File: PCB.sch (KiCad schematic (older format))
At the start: 62 parts, among them J1 PASSIVE_CHANNELS, J10 USB_RASPBERRY, J11 USB_ARDUINO, J12 100W_ch+, J13 100W_ch-, J14 100W_sense, J2 PASSIVE_CHANNELS, J3 PASSIVE_CHANNELS, J4 12V+, J5 12V-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

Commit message: Placement canal passif intial
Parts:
- renumbered J3 to J1, J1 to J2, J2 to J3
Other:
- moved on the sheet: J1, J2
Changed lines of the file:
@@
 $EndComp
 $Comp
-L Connector:Screw_Terminal_01x16 J2
+L Connector:Screw_Terminal_01x16 J3
 U 1 1 5F3E87B3
 P 1200 16150
-F 0 "J2" H 1118 17067 50  0000 C CNN
+F 0 "J3" H 1118 17067 50  0000 C CNN
 F 1 "PASSIVE_CHANNELS" H 1118 16976 50  0000 C CNN
 F 2 "TerminalBlock_Phoenix:TerminalBlock_Phoenix_PT-1,5-16-5.0-H_1x16_P5.00mm_Horizontal" H 1200 16150 50  0001 C CNN
@@
 $EndComp
 $Comp
-L Connector:Screw_Terminal_01x16 J3
+L Connector:Screw_Terminal_01x16 J1
 U 1 1 5F02987D
-P 1400 3800
-F 0 "J3" H 1318 4717 50  0000 C CNN
-F 1 "PASSIVE_CHANNELS" H 1318 4626 50  0000 C CNN
-F 2 "TerminalBlock_Phoenix:TerminalBlock_Phoenix_PT-1,5-16-5.0-H_1x16_P5.00mm_Horizontal" H 1400 3800 50  0001 C CNN
-F 3 "~" H 1400 3800 50  0001 C CNN
-	1    1400 3800
+P 850 2900
+F 0 "J1" H 768 3817 50  0000 C CNN
+F 1 "PASSIVE_CHANNELS" H 768 3726 50  0000 C CNN
+F 2 "TerminalBlock_Phoenix:TerminalBlock_Phoenix_PT-1,5-16-5.0-H_1x16_P5.00mm_Horizontal" H 850 2900 50  0001 C CNN
+F 3 "~" H 850 2900 50  0001 C CNN
+	1    850  2900
 	-1   0    0    -1
 $EndComp
@@
 T8-
 Wire Wire Line
-	1600 3100 1950 3100
-Wire Wire Line
-	1600 3200 1950 3200
-Text Label 1950 3100 0    50   ~ 0
+	1050 2200 1400 2200
+Wire Wire Line
+	1050 2300 1400 2300
+Text Label 1400 2200 0    50   ~ 0
 T1+
-Text Label 1950 3200 0    50   ~ 0
+Text Label 1400 2300 0    50   ~ 0
 T1-
 Wire Wire Line
-	1600 3300 1950 3300
-Wire Wire Line
-	1600 3400 1950 3400
-Text Label 1950 3300 0    50   ~ 0
+	1050 2400 1400 2400
+Wire Wire Line
+	1050 2500 1400 2500
+Text Label 1400 2400 0    50   ~ 0
 T2+
-Text Label 1950 3400 0    50   ~ 0
+Text Label 1400 2500 0    50   ~ 0
 T2-
 Wire Wire Line
-	1600 3500 1950 3500
-Wire Wire Line
-	1600 3600 1950 3600
-Text Label 1950 3500 0    50   ~ 0
+	1050 2600 1400 2600
+Wire Wire Line
+	1050 2700 1400 2700
+Text Label 1400 2600 0    50   ~ 0
 T3+
-Text Label 1950 3600 0    50   ~ 0
+Text Label 1400 2700 0    50   ~ 0
 T3-
 Wire Wire Line
-	1600 3700 1950 3700
-Wire Wire Line
-	1600 3800 1950 3800
-Text Label 1950 3700 0    50   ~ 0
+	1050 2800 1400 2800
+Wire Wire Line
+	1050 2900 1400 2900
+Text Label 1400 2800 0    50   ~ 0
 T4+
-Text Label 1950 3800 0    50   ~ 0
+Text Label 1400 2900 0    50   ~ 0
 T4-
 Wire Wire Line
-	1600 3900 1950 3900
-Wire Wire Line
-	1600 4000 1950 4000
-Text Label 1950 3900 0    50   ~ 0
+	1050 3000 1400 3000
+Wire Wire Line
+	1050 3100 1400 3100
+Text Label 1400 3000 0    50   ~ 0
 T5+
-Text Label 1950 4000 0    50   ~ 0
+Text Label 1400 3100 0    50   ~ 0
 T5-
 Wire Wire Line
-	1600 4100 1950 4100
-Wire Wire Line
-	1600 4200 1950 4200
-Text Label 1950 4100 0    50   ~ 0
+	1050 3200 1400 3200
+Wire Wire Line
+	1050 3300 1400 3300
+Text Label 1400 3200 0    50   ~ 0
 T6+
-Text Label 1950 4200 0    50   ~ 0
+Text Label 1400 3300 0    50   ~ 0
 T6-
 Wire Wire Line
-	1600 4300 1950 4300
-Wire Wire Line
-	1600 4400 1950 4400
-Text Label 1950 4300 0    50   ~ 0
+	1050 3400 1400 3400
+Wire Wire Line
+	1050 3500 1400 3500
+Text Label 1400 3400 0    50   ~ 0
 T7+
-Text Label 1950 4400 0    50   ~ 0
+Text Label 1400 3500 0    50   ~ 0
 T7-
 Wire Wire Line
-	1600 4500 1950 4500
-Wire Wire Line
-	1600 4600 1950 4600
-Text Label 1950 4500 0    50   ~ 0
+	1050 3600 1400 3600
+Wire Wire Line
+	1050 3700 1400 3700
+Text Label 1400 3600 0    50   ~ 0
 T8+
-Text Label 1950 4600 0    50   ~ 0
+Text Label 1400 3700 0    50   ~ 0
 T8-
 $Comp
-L Connector:Screw_Terminal_01x16 J1
+L Connector:Screw_Terminal_01x16 J2
 U 1 1 5F91A19D
-P 1100 7900
-F 0 "J1" H 1018 8817 50  0000 C CNN
-F 1 "PASSIVE_CHANNELS" H 1018 8726 50  0000 C CNN
-F 2 "TerminalBlock_Phoenix:TerminalBlock_Phoenix_PT-1,5-16-5.0-H_1x16_P5.00mm_Horizontal" H 1100 7900 50  0001 C CNN
-F 3 "~" H 1100 7900 50  0001 C CNN
-	1    1100 7900
+P 850 4800
+F 0 "J2" H 768 5717 50  0000 C CNN
+F 1 "PASSIVE_CHANNELS" H 768 5626 50  0000 C CNN
+F 2 "TerminalBlock_Phoenix:TerminalBlock_Phoenix_PT-1,5-16-5.0-H_1x16_P5.00mm_Horizontal" H 850 4800 50  0001 C CNN
+F 3 "~" H 850 4800 50  0001 C CNN
+	1    850  4800
 	-1   0    0    -1
 $EndComp
 Wire Wire Line
-	1300 7200 1650 7200
-Wire Wire Line
-	1300 7300 1650 7300
-Text Label 1650 7200 0    50   ~ 0
+	1050 4100 1400 4100
+Wire Wire Line
+	1050 4200 1400 4200
+Text Label 1400 4100 0    50   ~ 0
 T9+
-Text Label 1650 7300 0    50   ~ 0
+Text Label 1400 4200 0    50   ~ 0
 T9-
 Wire Wire Line
-	1300 7400 1650 7400
-Wire Wire Line
-	1300 7500 1650 7500
-Text Label 1650 7400 0    50   ~ 0
+	1050 4300 1400 4300
+Wire Wire Line
+	1050 4400 1400 4400
+Text Label 1400 4300 0    50   ~ 0
 T10+
-Text Label 1650 7500 0    50   ~ 0
+Text Label 1400 4400 0    50   ~ 0
 T10-
 Wire Wire Line
-	1300 7600 1650 7600
-Wire Wire Line
-	1300 7700 1650 7700
-Text Label 1650 7600 0    50   ~ 0
+	1050 4500 1400 4500
+Wire Wire Line
+	1050 4600 1400 4600
+Text Label 1400 4500 0    50   ~ 0
 T11+
-Text Label 1650 7700 0    50   ~ 0
+Text Label 1400 4600 0    50   ~ 0
 T11-
 Wire Wire Line
-	1300 7800 1650 7800
-Wire Wire Line
-	1300 7900 1650 7900
-Text Label 1650 7800 0    50   ~ 0
+	1050 4700 1400 4700
+Wire Wire Line
+	1050 4800 1400 4800
+Text Label 1400 4700 0    50   ~ 0
 T12+
-Text Label 1650 7900 0    50   ~ 0
+Text Label 1400 4800 0    50   ~ 0
 T12-
 Wire Wire Line
-	1300 8000 1650 8000
-Wire Wire Line
-	1300 8100 1650 8100
-Text Label 1650 8000 0    50   ~ 0
+	1050 4900 1400 4900
+Wire Wire Line
+	1050 5000 1400 5000
+Text Label 1400 4900 0    50   ~ 0
 T13+
-Text Label 1650 8100 0    50   ~ 0
+Text Label 1400 5000 0    50   ~ 0
 T13-
 Wire Wire Line
-	1300 8200 1650 8200
-Wire Wire Line
-	1300 8300 1650 8300
-Text Label 1650 8200 0    50   ~ 0
+	1050 5100 1400 5100
+Wire Wire Line
+	1050 5200 1400 5200
+Text Label 1400 5100 0    50   ~ 0
 T14+
-Text Label 1650 8300 0    50   ~ 0
+Text Label 1400 5200 0    50   ~ 0
 T14-
 Wire Wire Line
-	1300 8400 1650 8400
-Wire Wire Line
-	1300 8500 1650 8500
-Text Label 1650 8400 0    50   ~ 0
+	1050 5300 1400 5300
+Wire Wire Line
+	1050 5400 1400 5400
+Text Label 1400 5300 0    50   ~ 0
 T15+
-Text Label 1650 8500 0    50   ~ 0
+Text Label 1400 5400 0    50   ~ 0
 T15-
 Wire Wire Line
-	1300 8600 1650 8600
-Wire Wire Line
-	1300 8700 1650 8700
-Text Label 1650 8600 0    50   ~ 0
+	1050 5500 1400 5500
+Wire Wire Line
+	1050 5600 1400 5600
+Text Label 1400 5500 0    50   ~ 0
 T16+
-Text Label 1650 8700 0    50   ~ 0
+Text Label 1400 5600 0    50   ~ 0
 T16-
 Wire Wire Line

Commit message: Defi releve!
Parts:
- D1: footprint Package_TO_SOT_SMD:TO-277A -> PCB:TO-277A
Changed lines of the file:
@@
 F 0 "D1" H 11750 2915 50  0000 C CNN
 F 1 "FSV1045V" H 11750 2824 50  0000 C CNN
-F 2 "Package_TO_SOT_SMD:TO-277A" H 11750 2650 50  0001 C CNN
+F 2 "PCB:TO-277A" H 11750 2650 50  0001 C CNN
 F 3 "~" H 11750 2650 50  0001 C CNN
 	1    11750 2650

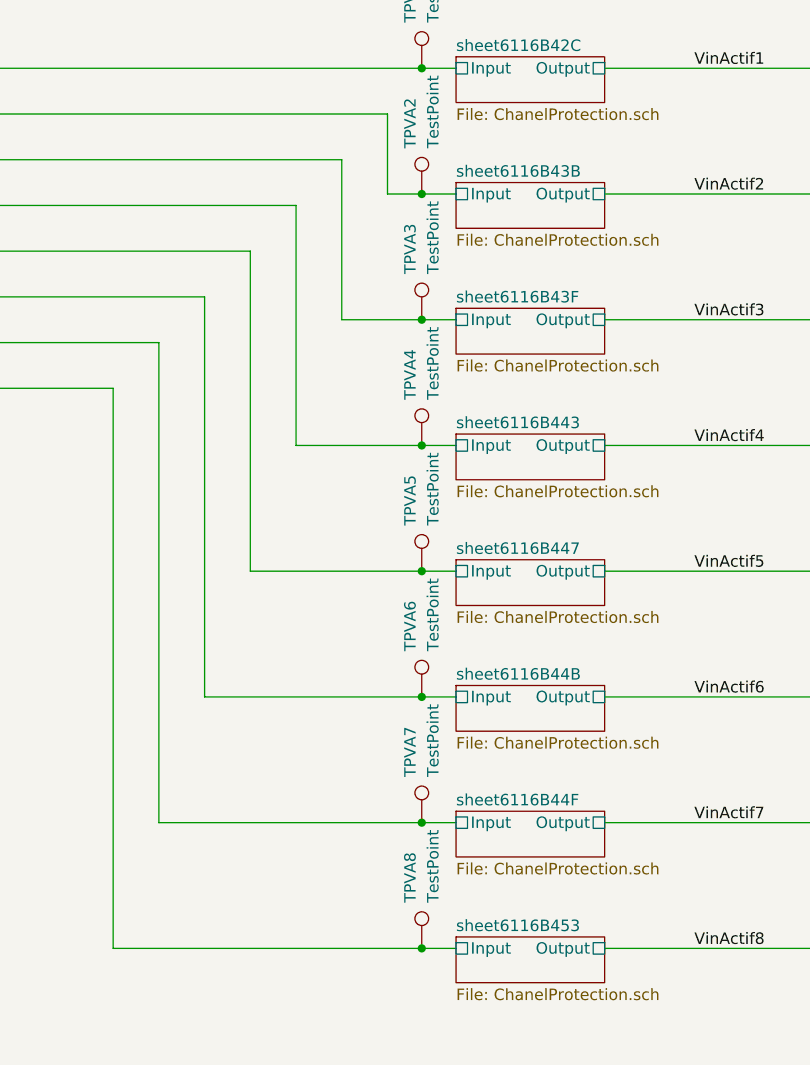
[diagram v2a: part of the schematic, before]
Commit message: Petit ajustement pour accomoder le usb du arduino, pret pour routing
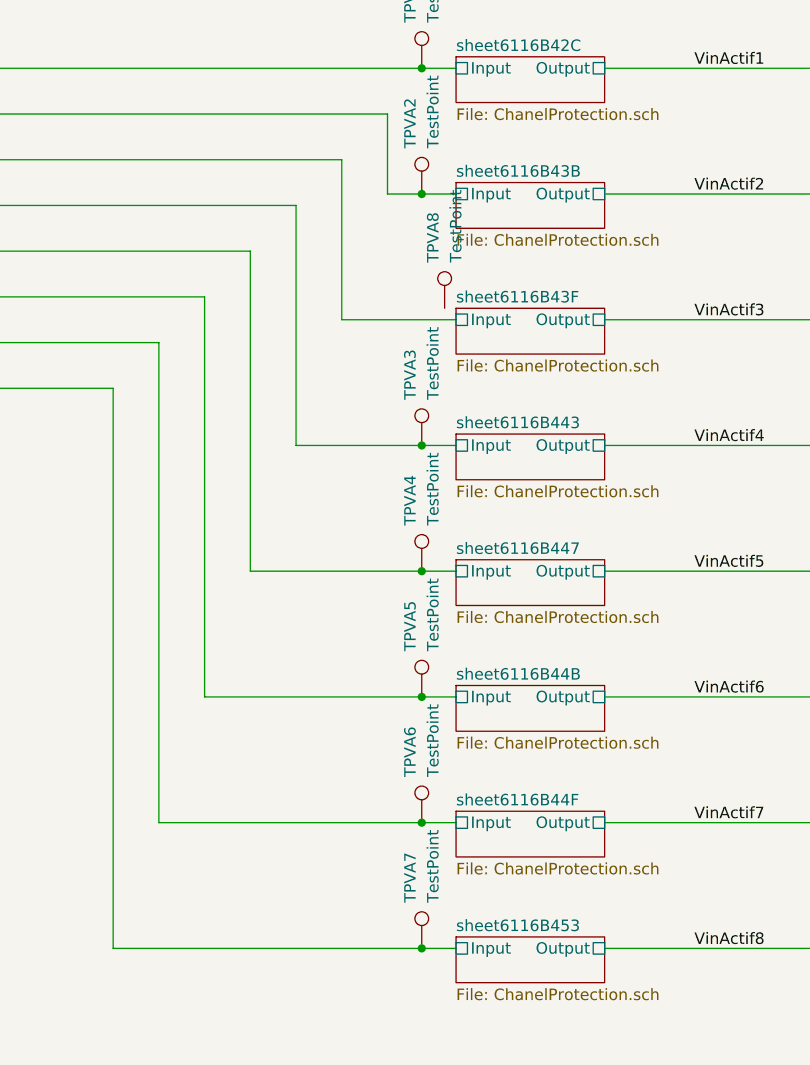
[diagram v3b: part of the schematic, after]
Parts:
- renumbered TPVA4 to TPVA3, TPVA5 to TPVA4, TPVA6 to TPVA5, TPVA7 to TPVA6, TPVA8 to TPVA7, TPVA3 to TPVA8
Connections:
- net sheet6116B43F/Input: no longer TPVA8.1
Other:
- moved on the sheet: TPVA8
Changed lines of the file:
@@
 L Connector:TestPoint TPVA?
 U 1 1 6116B3F2
-P 18450 16850
+P 18550 16800
 AR Path="/5EBDFBAE/6116B3F2" Ref="TPVA?"  Part="1"
 AR Path="/5EC0778F/6116B3F2" Ref="TPVA?"  Part="1"
@@
 AR Path="/5F466B56/6116B3F2" Ref="TPVA?"  Part="1"
 AR Path="/5F466B61/6116B3F2" Ref="TPVA?"  Part="1"
-AR Path="/6116B3F2" Ref="TPVA3"  Part="1"
-F 0 "TPVA3" V 18400 17050 50  0000 L CNN
-F 1 "TestPoint" V 18500 17050 50  0000 L CNN
-F 2 "TestPoint:TestPoint_Pad_1.0x1.0mm" H 18650 16850 50  0001 C CNN
-F 3 "~" H 18650 16850 50  0001 C CNN
-	1    18450 16850
+AR Path="/6116B3F2" Ref="TPVA8"  Part="1"
+F 0 "TPVA8" V 18500 17000 50  0000 L CNN
+F 1 "TestPoint" V 18600 17000 50  0000 L CNN
+F 2 "TestPoint:TestPoint_Pad_1.0x1.0mm" H 18750 16800 50  0001 C CNN
+F 3 "~" H 18750 16800 50  0001 C CNN
+	1    18550 16800
 	1    0    0    -1
 $EndComp
@@
 AR Path="/5F466B56/6116B3FC" Ref="TPVA?"  Part="1"
 AR Path="/5F466B61/6116B3FC" Ref="TPVA?"  Part="1"
-AR Path="/6116B3FC" Ref="TPVA4"  Part="1"
-F 0 "TPVA4" V 18400 17600 50  0000 L CNN
+AR Path="/6116B3FC" Ref="TPVA3"  Part="1"
+F 0 "TPVA3" V 18400 17600 50  0000 L CNN
 F 1 "TestPoint" V 18500 17600 50  0000 L CNN
 F 2 "TestPoint:TestPoint_Pad_1.0x1.0mm" H 18650 17400 50  0001 C CNN
@@
 AR Path="/5F466B56/6116B406" Ref="TPVA?"  Part="1"
 AR Path="/5F466B61/6116B406" Ref="TPVA?"  Part="1"
-AR Path="/6116B406" Ref="TPVA5"  Part="1"
-F 0 "TPVA5" V 18400 18150 50  0000 L CNN
+AR Path="/6116B406" Ref="TPVA4"  Part="1"
+F 0 "TPVA4" V 18400 18150 50  0000 L CNN
 F 1 "TestPoint" V 18500 18150 50  0000 L CNN
 F 2 "TestPoint:TestPoint_Pad_1.0x1.0mm" H 18650 17950 50  0001 C CNN
@@
 AR Path="/5F466B56/6116B410" Ref="TPVA?"  Part="1"
 AR Path="/5F466B61/6116B410" Ref="TPVA?"  Part="1"
-AR Path="/6116B410" Ref="TPVA6"  Part="1"
-F 0 "TPVA6" V 18400 18700 50  0000 L CNN
+AR Path="/6116B410" Ref="TPVA5"  Part="1"
+F 0 "TPVA5" V 18400 18700 50  0000 L CNN
 F 1 "TestPoint" V 18500 18700 50  0000 L CNN
 F 2 "TestPoint:TestPoint_Pad_1.0x1.0mm" H 18650 18500 50  0001 C CNN
@@
 AR Path="/5F466B56/6116B41A" Ref="TPVA?"  Part="1"
 AR Path="/5F466B61/6116B41A" Ref="TPVA?"  Part="1"
-AR Path="/6116B41A" Ref="TPVA7"  Part="1"
-F 0 "TPVA7" V 18400 19250 50  0000 L CNN
+AR Path="/6116B41A" Ref="TPVA6"  Part="1"
+F 0 "TPVA6" V 18400 19250 50  0000 L CNN
 F 1 "TestPoint" V 18500 19250 50  0000 L CNN
 F 2 "TestPoint:TestPoint_Pad_1.0x1.0mm" H 18650 19050 50  0001 C CNN
@@
 AR Path="/5F466B56/6116B424" Ref="TPVA?"  Part="1"
 AR Path="/5F466B61/6116B424" Ref="TPVA?"  Part="1"
-AR Path="/6116B424" Ref="TPVA8"  Part="1"
-F 0 "TPVA8" V 18400 19800 50  0000 L CNN
+AR Path="/6116B424" Ref="TPVA7"  Part="1"
+F 0 "TPVA7" V 18400 19800 50  0000 L CNN
 F 1 "TestPoint" V 18500 19800 50  0000 L CNN
 F 2 "TestPoint:TestPoint_Pad_1.0x1.0mm" H 18650 19600 50  0001 C CNN
@@
 	18300 16300 18450 16300
 Wire Wire Line
-	18100 16850 18450 16850
-Wire Wire Line
 	18600 17400 18450 17400
 Wire Wire Line
@@
 Wire Wire Line
 	18450 16300 18600 16300
-Connection ~ 18450 16850
-Wire Wire Line
-	18450 16850 18600 16850
 Connection ~ 18450 17400
 Wire Wire Line
@@
 Wire Wire Line
 	36850 4600 36950 4600
+Wire Wire Line
+	18100 16850 18600 16850
 $EndSCHEMATC

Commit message: Debug routing
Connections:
- net +5VPI: no longer J9.1 (Pin_1)
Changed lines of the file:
@@
 	1    0    0    -1
 $EndComp
-Text Label 18200 4450 0    50   ~ 0
-+5VPI
 Wire Wire Line
 	18200 4450 18050 4450
@@
 	1    0    0    -1
 $EndComp
-Text Label 18850 4450 2    50   ~ 0
-+5VPI
 Wire Wire Line
 	19150 4450 18850 4450
@@
 Wire Wire Line
 	18100 16850 18600 16850
+Text Label 18200 4450 0    50   ~ 0
++5VPI
 $EndSCHEMATC

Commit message: retrait des test points inutiles
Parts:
- removed TPVA1, TPVA2, TPVA3, TPVA4, TPVA5, TPVA6, TPVA7, TPVA8, TPVP1, TPVP2, TPVP3, TPVP4, TPVP5, TPVP6, TPVP7, TPVP8: TestPoint, TestPoint:TestPoint_Pad_1.0x1.0mm, symbol Connector:TestPoint

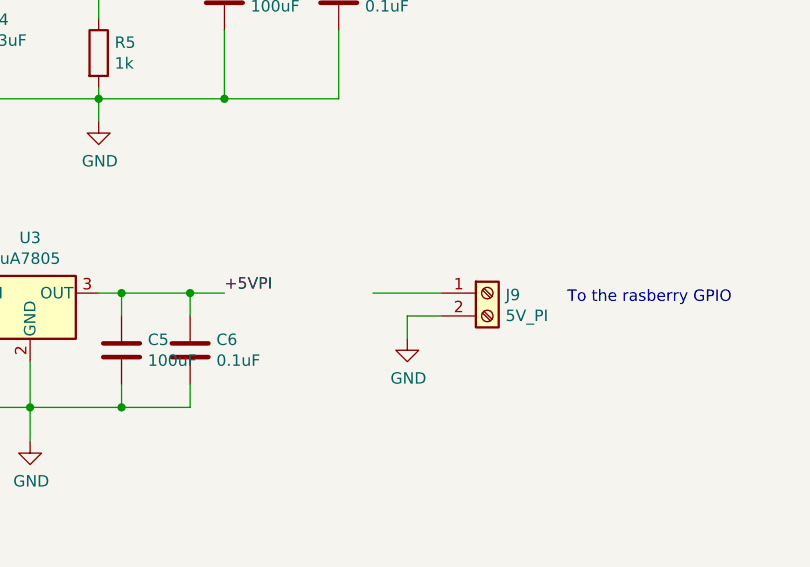
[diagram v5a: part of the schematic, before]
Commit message: Routed most of the power
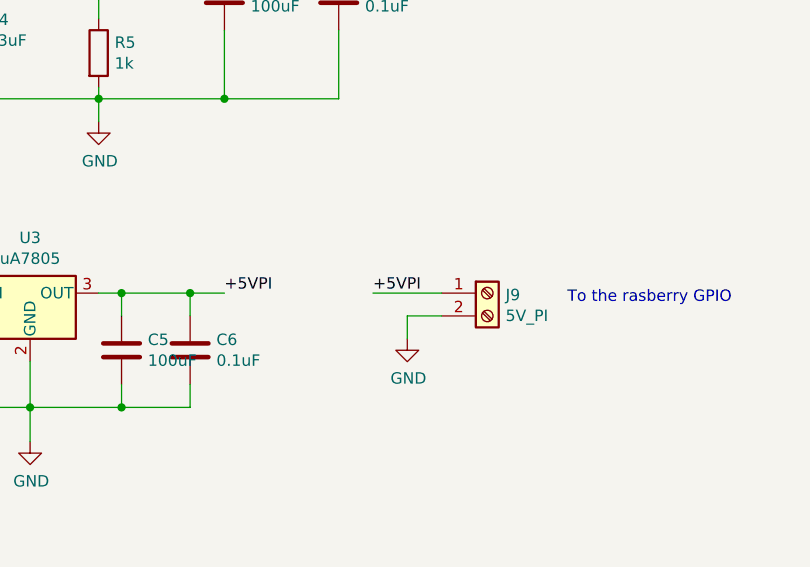
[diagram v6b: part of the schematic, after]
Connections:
- net +5VPI: now also J9.1 (Pin_1)
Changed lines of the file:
@@
 Wire Wire Line
 	2250 19300 3750 19300
+Text Label 18850 4450 0    50   ~ 0
++5VPI
 $EndSCHEMATC

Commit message: routing usb
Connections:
- net D-: now reaches J10.2 (D-), J11.2 (D-)
- net D+: now reaches J10.3 (D+), J11.3 (D+)
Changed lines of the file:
@@
 Text Label 18850 4450 0    50   ~ 0
 +5VPI
+Text Label 24900 3250 0    50   ~ 0
+D+
+Text Label 24950 3350 0    50   ~ 0
+D-
 $EndSCHEMATC

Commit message: Ajustement placement canaux actifs
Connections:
- net sheet6116B42C/Input renamed ProtectionActif1/Input
- net sheet6116B43B/Input renamed ProtectionActif2/Input
- net sheet6116B43F/Input renamed ProtectionActif3/Input
- net sheet6116B443/Input renamed ProtectionActif4/Input
- net sheet6116B447/Input renamed ProtectionActif5/Input
- net sheet6116B44B/Input renamed ProtectionActif6/Input
- net sheet6116B44F/Input renamed ProtectionActif7/Input
- net sheet6116B453/Input renamed ProtectionActif8/Input
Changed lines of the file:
@@
 S 18600 15700 650  200
 U 6116B42C
-F0 "sheet6116B42C" 50
+F0 "ProtectionActif1" 50
 F1 "ChanelProtection.sch" 50
 F2 "Input" U L 18600 15750 50
@@
 S 18600 16250 650  200
 U 6116B43B
-F0 "sheet6116B43B" 50
+F0 "ProtectionActif2" 50
 F1 "ChanelProtection.sch" 50
 F2 "Input" U L 18600 16300 50
@@
 S 18600 16800 650  200
 U 6116B43F
-F0 "sheet6116B43F" 50
+F0 "ProtectionActif3" 50
 F1 "ChanelProtection.sch" 50
 F2 "Input" U L 18600 16850 50
@@
 S 18600 17350 650  200
 U 6116B443
-F0 "sheet6116B443" 50
+F0 "ProtectionActif4" 50
 F1 "ChanelProtection.sch" 50
 F2 "Input" U L 18600 17400 50
@@
 S 18600 17900 650  200
 U 6116B447
-F0 "sheet6116B447" 50
+F0 "ProtectionActif5" 50
 F1 "ChanelProtection.sch" 50
 F2 "Input" U L 18600 17950 50
@@
 S 18600 18450 650  200
 U 6116B44B
-F0 "sheet6116B44B" 50
+F0 "ProtectionActif6" 50
 F1 "ChanelProtection.sch" 50
 F2 "Input" U L 18600 18500 50
@@
 S 18600 19000 650  200
 U 6116B44F
-F0 "sheet6116B44F" 50
+F0 "ProtectionActif7" 50
 F1 "ChanelProtection.sch" 50
 F2 "Input" U L 18600 19050 50
@@
 S 18600 19550 650  200
 U 6116B453
-F0 "sheet6116B453" 50
+F0 "ProtectionActif8" 50
 F1 "ChanelProtection.sch" 50
 F2 "Input" U L 18600 19600 50
